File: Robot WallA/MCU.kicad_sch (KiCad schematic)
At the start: 0 parts

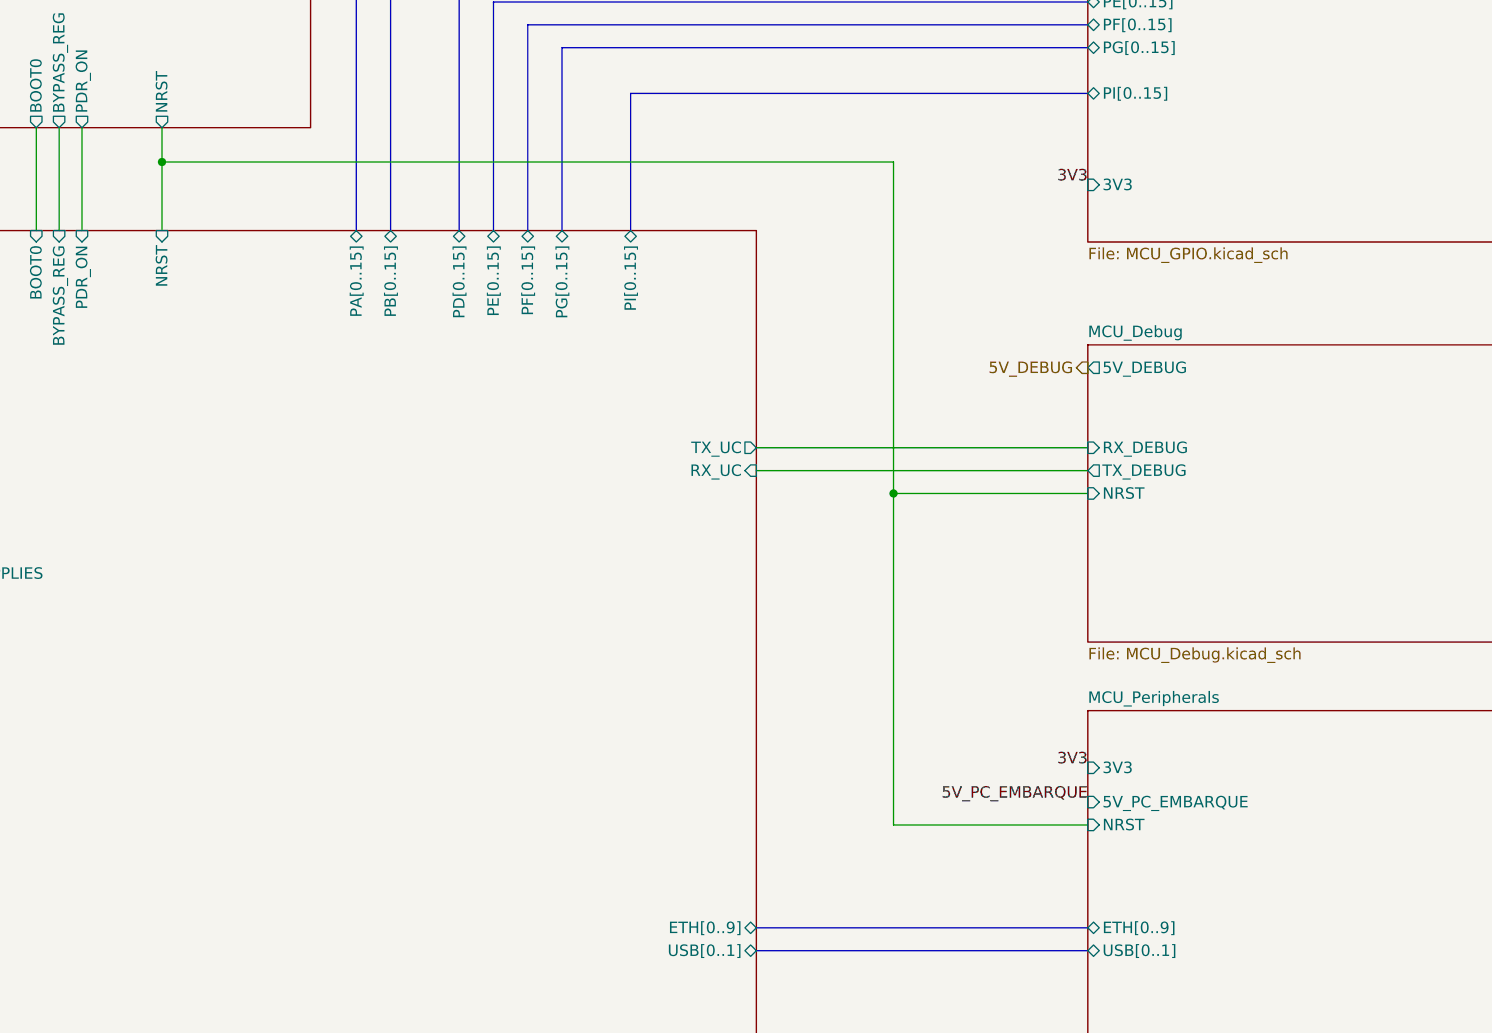
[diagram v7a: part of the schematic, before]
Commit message: Added diode for Type-C connector in case we accidentally power the board with this connector.
Updated fab files
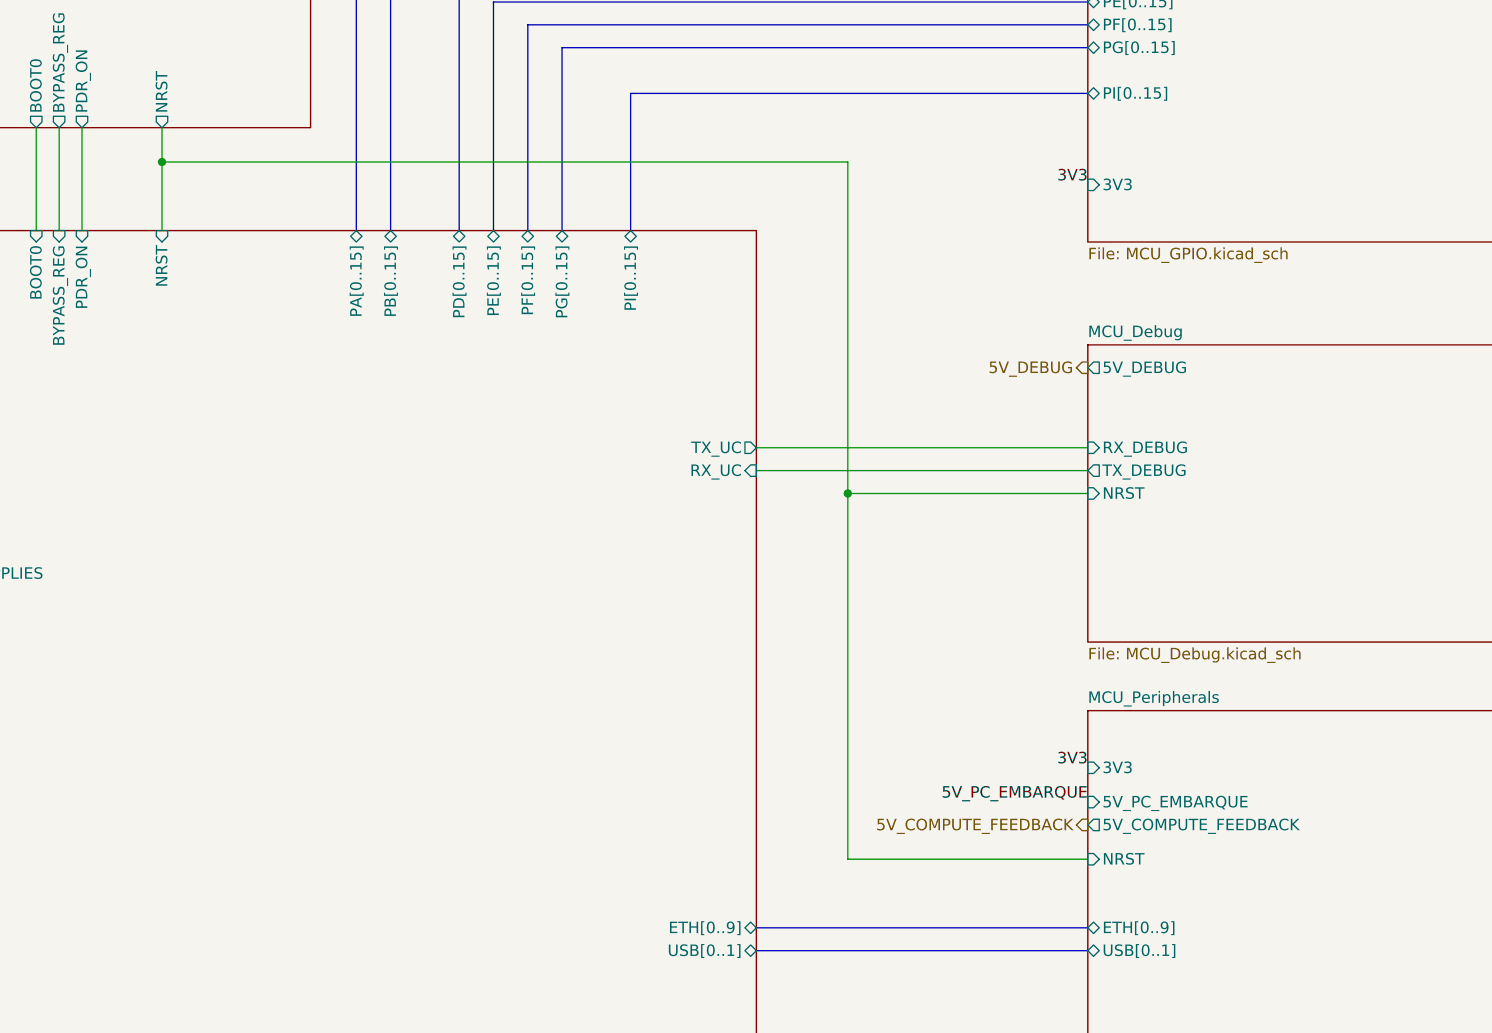
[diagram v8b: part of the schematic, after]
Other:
- sheet MCU_Peripherals ports: added 5V_COMPUTE_FEEDBACK; removed none
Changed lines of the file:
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@@
-	)
-	(junction
-		(at 172.72 93.98)
-		(diameter 0)
-		(color 0 0 0 0)
 	)
 	(junction
@@
 		(color 0 0 0 0)
 	)
+	(junction
+		(at 167.64 93.98)
+		(diameter 0)
+		(color 0 0 0 0)
+	)
 	(bus
 		(pts
@@
 	(wire
 		(pts
-			(xy 172.72 93.98) (xy 194.31 93.98)
-		)
-		(stroke
-			(width 0)
-			(type default)
-		)
-	)
-	(wire
-		(pts
 			(xy 157.48 91.44) (xy 194.31 91.44)
 		)
@@
 		)
 	)
-	(wire
-		(pts
-			(xy 172.72 130.81) (xy 194.31 130.81)
-		)
-		(stroke
-			(width 0)
-			(type default)
-		)
-	)
 	(bus
 		(pts
@@
 		)
 	)
+	(wire
+		(pts
+			(xy 167.64 93.98) (xy 194.31 93.98)
+		)
+		(stroke
+			(width 0)
+			(type default)
+		)
+	)
 	(bus
 		(pts
@@
 		)
 	)
+	(wire
+		(pts
+			(xy 167.64 93.98) (xy 167.64 134.62)
+		)
+		(stroke
+			(width 0)
+			(type default)
+		)
+	)
 	(bus
 		(pts
@@
 	(wire
 		(pts
-			(xy 91.44 57.15) (xy 172.72 57.15)
+			(xy 91.44 57.15) (xy 167.64 57.15)
 		)
 		(stroke
@@
 	(wire
 		(pts
-			(xy 172.72 93.98) (xy 172.72 130.81)
+			(xy 167.64 134.62) (xy 194.31 134.62)
 		)
 		(stroke
@@
 	(wire
 		(pts
-			(xy 172.72 57.15) (xy 172.72 93.98)
+			(xy 167.64 57.15) (xy 167.64 93.98)
 		)
 		(stroke
@@
 		(shape input)
 		(at 48.26 105.41 180)
+		(effects
+			(font
+				(size 1.27 1.27)
+			)
+			(justify right)
+		)
+	)
+	(hierarchical_label "5V_COMPUTE_FEEDBACK"
+		(shape output)
+		(at 194.31 130.81 180)
 		(effects
 			(font
@@
 		)
 		(pin "NRST" input
-			(at 194.31 130.81 180)
+			(at 194.31 134.62 180)
 			(effects
 				(font
@@
 			(effects
 				(font
+					(size 1.27 1.27)
+				)
+				(justify left)
+			)
+		)
+		(pin "5V_COMPUTE_FEEDBACK" output
+			(at 194.31 130.81 180)
+			(effects
+				(font
